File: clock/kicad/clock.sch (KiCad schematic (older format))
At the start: 106 parts, among them J1 USB-SS-52100-001, Q1 PN2222A, SW1 HOUR, SW2 MIN, SW3 TIME, U1 74HC4060, U10 74HC4511, U11 74HC4511, U12 74HC4511, U13 74HC4511, U14 KCSC02-105, U15 KCSC02-105, U16 KCSC02-105, U17 KCSC02-105, U18 KCSC02-105, U19 KCSC02-105, U2 SN74HC74N, U20 74HC14, U21 74HC157, U22 NE555P, U3 74HC390, U4 74HC08, U5 74HC390, U6 74HC08, U7 74HC390, U8 74HC4511, U9 74HC4511

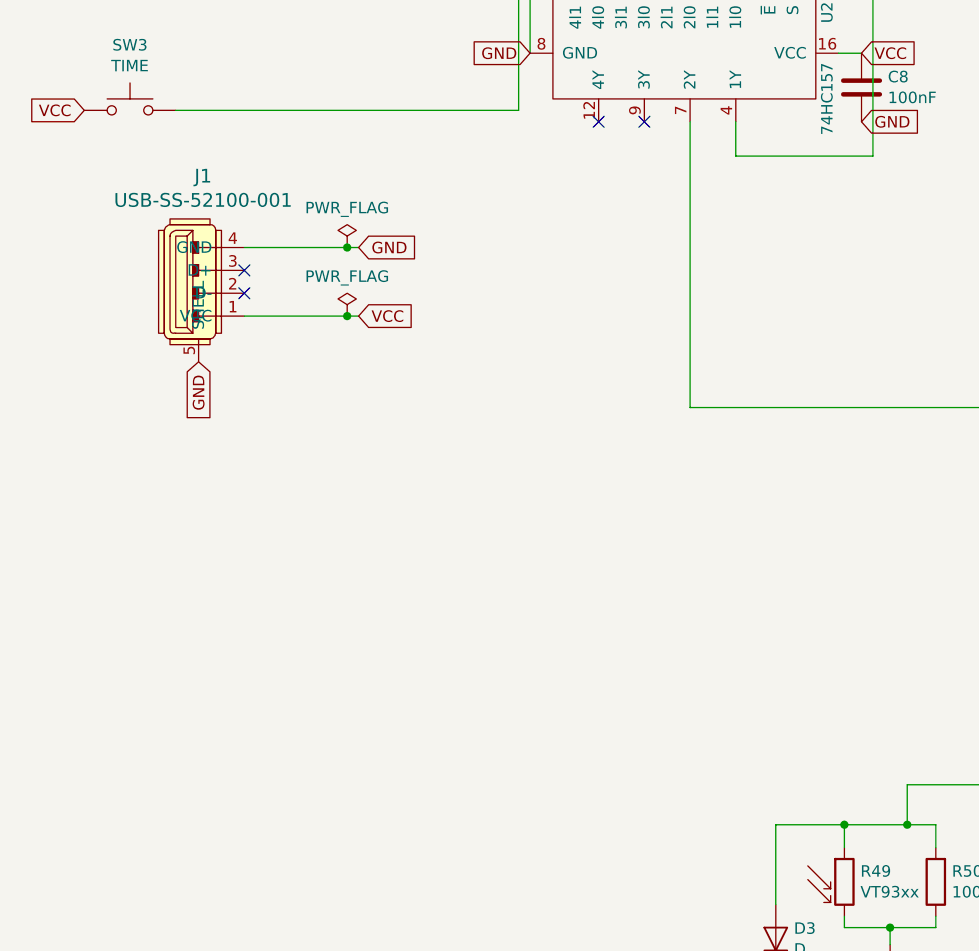
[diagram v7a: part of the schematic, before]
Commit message: Clock: Added adjustable voltage regulator.
Switched the circuit from 5v to 3v to match the crystal's recommended
schematic.
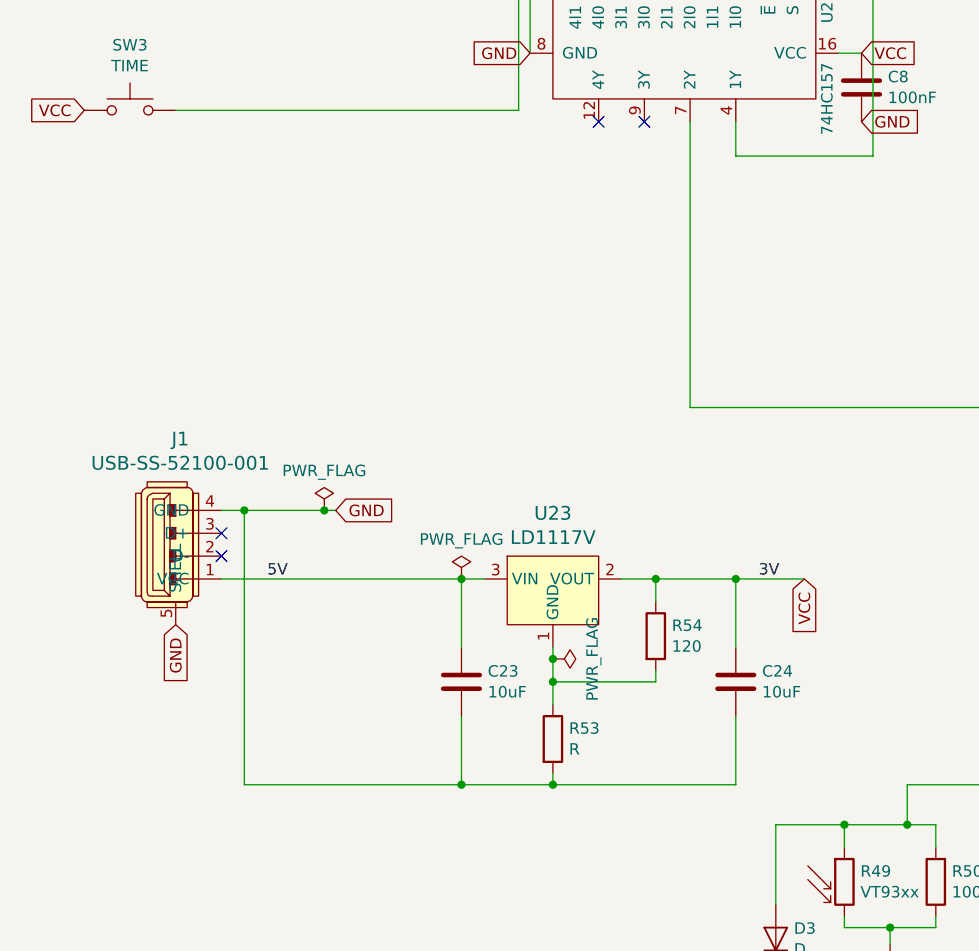
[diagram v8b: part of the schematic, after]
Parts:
- added C23, C24: 10uF, symbol Device:C
- added R53: R, symbol Device:R
- added R54: 120, symbol Device:R
- added U23: LD1117V, digikey-footprints:TO-220-3, symbol clock:LD1117V
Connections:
- net GND: now also C23.2, C24.2, R53.2
- net VCC: now also C24.1, R54.1, U23.2 (VOUT); no longer J1.1 (VCC)
- new net: R53.1, R54.2, U23.1 (GND)
- new net 5V: C23.1, J1.1 (VCC), U23.3 (VIN)
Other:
- moved on the sheet: J1
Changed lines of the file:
@@
 Wire Wire Line
 	3600 5850 3600 5700
-Text GLabel 2150 8300 2    50   Input ~ 0
+Text GLabel 4100 9450 3    50   Input ~ 0
 VCC
-Text GLabel 2150 8000 2    50   Input ~ 0
-GND
-Wire Wire Line
-	2150 8300 2100 8300
-$Comp
-L power:PWR_FLAG #FLG0101
-U 1 1 5D14D41D
-P 2100 8300
-F 0 "#FLG0101" H 2100 8375 50  0001 C CNN
-F 1 "PWR_FLAG" H 2100 8473 50  0000 C CNN
-F 2 "" H 2100 8300 50  0001 C CNN
-F 3 "~" H 2100 8300 50  0001 C CNN
-	1    2100 8300
-	1    0    0    -1
-$EndComp
-Connection ~ 2100 8300
+Text GLabel 2050 9150 2    50   Input ~ 0
+GND
 $Comp
 L power:PWR_FLAG #FLG0102
 U 1 1 5D2210FE
-P 2100 8000
-F 0 "#FLG0102" H 2100 8075 50  0001 C CNN
-F 1 "PWR_FLAG" H 2100 8173 50  0000 C CNN
-F 2 "" H 2100 8000 50  0001 C CNN
-F 3 "~" H 2100 8000 50  0001 C CNN
-	1    2100 8000
-	1    0    0    -1
-$EndComp
-Connection ~ 2100 8000
-Wire Wire Line
-	2100 8000 2150 8000
+P 2000 9150
+F 0 "#FLG0102" H 2000 9225 50  0001 C CNN
+F 1 "PWR_FLAG" H 2000 9323 50  0000 C CNN
+F 2 "" H 2000 9150 50  0001 C CNN
+F 3 "~" H 2000 9150 50  0001 C CNN
+	1    2000 9150
+	1    0    0    -1
+$EndComp
+Connection ~ 2000 9150
+Wire Wire Line
+	2000 9150 2050 9150
 Wire Wire Line
 	3550 5750 3550 6700
@@
 Wire Wire Line
 	3200 1050 4100 1050
-Wire Wire Line
-	1650 8000 2100 8000
-Wire Wire Line
-	1650 8300 2100 8300
-NoConn ~ 1650 8100
-NoConn ~ 1650 8200
-Text GLabel 1450 8500 3    50   Input ~ 0
+NoConn ~ 1550 9250
+NoConn ~ 1550 9350
+Text GLabel 1350 9650 3    50   Input ~ 0
 GND
 $Comp
 L clock:USB-SS-52100-001 J1
 U 1 1 5D8F04E6
-P 1350 8200
-F 0 "J1" H 1470 8712 60  0000 C CNN
-F 1 "USB-SS-52100-001" H 1470 8606 60  0000 C CNN
-F 2 "KiCad:USB_A_Stewart_SS-52100-001_Horizontal" H 1550 8400 60  0001 L CNN
-F 3 "https://belfuse.com/resources/drawings/stewartconnector/dr-stw-ss-52100-001.pdf" H 1550 8500 60  0001 L CNN
-F 4 "380-1412-ND" H 1550 8600 60  0001 L CNN "Digi-Key_PN"
-F 5 "SS-52100-001" H 1550 8700 60  0001 L CNN "MPN"
-F 6 "Connectors, Interconnects" H 1550 8800 60  0001 L CNN "Category"
-F 7 "USB, DVI, HDMI Connectors" H 1550 8900 60  0001 L CNN "Family"
-F 8 "https://www.digikey.com/product-detail/en/stewart-connector/SS-52100-001/380-1412-ND/7902377" H 1550 9100 60  0001 L CNN "DK_Detail_Page"
-F 9 "CONN RCPT USB2.0 TYPEA 4POS R/A" H 1550 9200 60  0001 L CNN "Description"
-F 10 "Stewart Connector" H 1550 9300 60  0001 L CNN "Manufacturer"
-F 11 "Active" H 1550 9400 60  0001 L CNN "Status"
-	1    1350 8200
+P 1250 9350
+F 0 "J1" H 1370 9862 60  0000 C CNN
+F 1 "USB-SS-52100-001" H 1370 9756 60  0000 C CNN
+F 2 "KiCad:USB_A_Stewart_SS-52100-001_Horizontal" H 1450 9550 60  0001 L CNN
+F 3 "https://belfuse.com/resources/drawings/stewartconnector/dr-stw-ss-52100-001.pdf" H 1450 9650 60  0001 L CNN
+F 4 "380-1412-ND" H 1450 9750 60  0001 L CNN "Digi-Key_PN"
+F 5 "SS-52100-001" H 1450 9850 60  0001 L CNN "MPN"
+F 6 "Connectors, Interconnects" H 1450 9950 60  0001 L CNN "Category"
+F 7 "USB, DVI, HDMI Connectors" H 1450 10050 60  0001 L CNN "Family"
+F 8 "https://www.digikey.com/product-detail/en/stewart-connector/SS-52100-001/380-1412-ND/7902377" H 1450 10250 60  0001 L CNN "DK_Detail_Page"
+F 9 "CONN RCPT USB2.0 TYPEA 4POS R/A" H 1450 10350 60  0001 L CNN "Description"
+F 10 "Stewart Connector" H 1450 10450 60  0001 L CNN "Manufacturer"
+F 11 "Active" H 1450 10550 60  0001 L CNN "Status"
+	1    1250 9350
 	1    0    0    -1
 $EndComp
@@
 	1    0    0    -1
 $EndComp
+$Comp
+L clock:LD1117V U23
+U 1 1 5D8CEEE4
+P 3000 9450
+F 0 "U23" H 3000 9737 60  0000 C CNN
+F 1 "LD1117V" H 3000 9631 60  0000 C CNN
+F 2 "digikey-footprints:TO-220-3" H 3200 9650 60  0001 L CNN
+F 3 "http://www.st.com/content/ccc/resource/technical/document/datasheet/99/3b/7d/91/91/51/4b/be/CD00000544.pdf/files/CD00000544.pdf/jcr:content/translations/en.CD00000544.pdf" H 3200 9750 60  0001 L CNN
+F 4 "497-7310-5-ND" H 3200 9850 60  0001 L CNN "Digi-Key_PN"
+F 5 "LD1117V" H 3200 9950 60  0001 L CNN "MPN"
+F 6 "Integrated Circuits (ICs)" H 3200 10050 60  0001 L CNN "Category"
+F 7 "PMIC - Voltage Regulators - Linear" H 3200 10150 60  0001 L CNN "Family"
+F 8 "http://www.st.com/content/ccc/resource/technical/document/datasheet/99/3b/7d/91/91/51/4b/be/CD00000544.pdf/files/CD00000544.pdf/jcr:content/translations/en.CD00000544.pdf" H 3200 10250 60  0001 L CNN "DK_Datasheet_Link"
+F 9 "/product-detail/en/stmicroelectronics/LD1117V33/497-1491-5-ND/586012" H 3200 10350 60  0001 L CNN "DK_Detail_Page"
+F 10 "IC REG LINEAR 1.8V-5V 800MA TO220AB" H 3200 10450 60  0001 L CNN "Description"
+F 11 "STMicroelectronics" H 3200 10550 60  0001 L CNN "Manufacturer"
+F 12 "Active" H 3200 10650 60  0001 L CNN "Status"
+	1    3000 9450
+	1    0    0    -1
+$EndComp
+$Comp
+L Device:C C23
+U 1 1 5D98A569
+P 2600 9900
+F 0 "C23" H 2715 9946 50  0000 L CNN
+F 1 "10uF" H 2715 9855 50  0000 L CNN
+F 2 "" H 2638 9750 50  0001 C CNN
+F 3 "~" H 2600 9900 50  0001 C CNN
+	1    2600 9900
+	1    0    0    -1
+$EndComp
+Wire Wire Line
+	1550 9150 1650 9150
+$Comp
+L Device:R R54
+U 1 1 5DA44C3B
+P 3450 9700
+F 0 "R54" H 3520 9746 50  0000 L CNN
+F 1 "120" H 3520 9655 50  0000 L CNN
+F 2 "" V 3380 9700 50  0001 C CNN
+F 3 "~" H 3450 9700 50  0001 C CNN
+	1    3450 9700
+	1    0    0    -1
+$EndComp
+$Comp
+L Device:R R53
+U 1 1 5DA450EA
+P 3000 10150
+F 0 "R53" H 3070 10196 50  0000 L CNN
+F 1 "R" H 3070 10105 50  0000 L CNN
+F 2 "" V 2930 10150 50  0001 C CNN
+F 3 "~" H 3000 10150 50  0001 C CNN
+	1    3000 10150
+	1    0    0    -1
+$EndComp
+Wire Wire Line
+	3450 9850 3450 9900
+Wire Wire Line
+	3450 9900 3000 9900
+Connection ~ 3000 9900
+Wire Wire Line
+	3000 9900 3000 10000
+Wire Wire Line
+	3300 9450 3450 9450
+Wire Wire Line
+	3450 9450 3450 9550
+Connection ~ 3450 9450
+$Comp
+L Device:C C24
+U 1 1 5DB38DC1
+P 3800 9900
+F 0 "C24" H 3915 9946 50  0000 L CNN
+F 1 "10uF" H 3915 9855 50  0000 L CNN
+F 2 "" H 3838 9750 50  0001 C CNN
+F 3 "~" H 3800 9900 50  0001 C CNN
+	1    3800 9900
+	1    0    0    -1
+$EndComp
+Wire Wire Line
+	2600 9750 2600 9450
+Connection ~ 2600 9450
+Wire Wire Line
+	2600 9450 2700 9450
+Wire Wire Line
+	3800 9750 3800 9450
+Wire Wire Line
+	3450 9450 3800 9450
+Wire Wire Line
+	3800 9450 4100 9450
+Connection ~ 3800 9450
+Wire Wire Line
+	3800 10050 3800 10350
+Wire Wire Line
+	3800 10350 3000 10350
+Wire Wire Line
+	1650 10350 1650 9150
+Connection ~ 1650 9150
+Wire Wire Line
+	1650 9150 2000 9150
+Wire Wire Line
+	2600 10050 2600 10350
+Connection ~ 2600 10350
+Wire Wire Line
+	2600 10350 1650 10350
+Wire Wire Line
+	3000 10300 3000 10350
+Connection ~ 3000 10350
+Wire Wire Line
+	3000 10350 2600 10350
+Wire Wire Line
+	1550 9450 2600 9450
+Text Label 3900 9450 0    50   ~ 0
+3V
+Text Label 1750 9450 0    50   ~ 0
+5V
+$Comp
+L power:PWR_FLAG #FLG0104
+U 1 1 5DD3A742
+P 2600 9450
+F 0 "#FLG0104" H 2600 9525 50  0001 C CNN
+F 1 "PWR_FLAG" H 2600 9623 50  0000 C CNN
+F 2 "" H 2600 9450 50  0001 C CNN
+F 3 "~" H 2600 9450 50  0001 C CNN
+	1    2600 9450
+	1    0    0    -1
+$EndComp
+$Comp
+L power:PWR_FLAG #FLG0101
+U 1 1 5D14D41D
+P 3000 9800
+F 0 "#FLG0101" H 3000 9875 50  0001 C CNN
+F 1 "PWR_FLAG" H 3000 9973 50  0000 C CNN
+F 2 "" H 3000 9800 50  0001 C CNN
+F 3 "~" H 3000 9800 50  0001 C CNN
+	1    3000 9800
+	0    1    1    0
+$EndComp
+Wire Wire Line
+	3000 9750 3000 9800
+Connection ~ 3000 9800
+Wire Wire Line
+	3000 9800 3000 9900
 $EndSCHEMATC
